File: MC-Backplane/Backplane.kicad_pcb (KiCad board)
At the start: 4 copper layers, 274.3 x 132.6 mm, 54 parts, among them J1 1730010, U1 64600001223, U10 86094328314755V1LF, U11 86094328314755V1LF, U12 374472, U13 86094328314755V1LF, U14 86094328314755V1LF, U2 SISS05DN-T1-GE3, U3 86094328314755V1LF, U4 86094328314755V1LF, U5 86094328314755V1LF, U6 86094328314755V1LF, U7 86094328314755V1LF, U8 86094328314755V1LF, U9 86094328314755V1LF

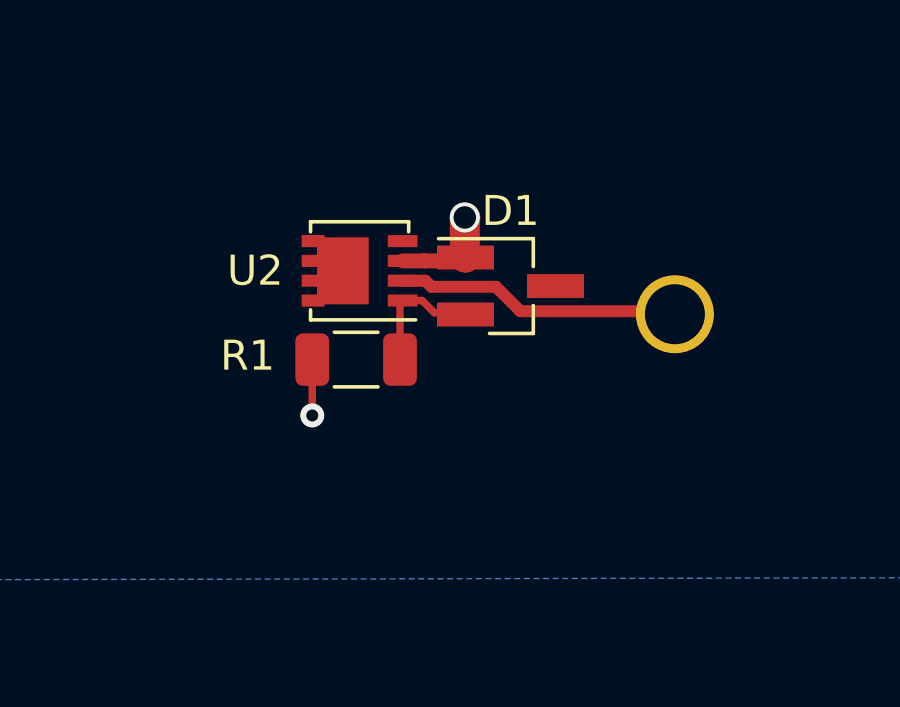
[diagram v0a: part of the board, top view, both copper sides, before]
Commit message: - updated PMOSFET&Zener footprint
reverse polarity protection circuit
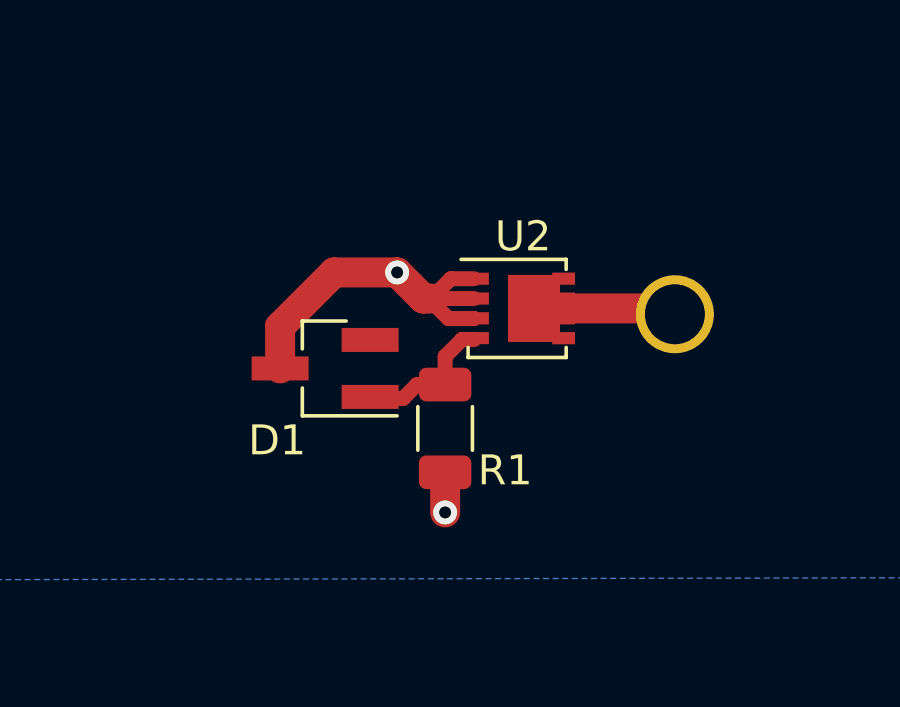
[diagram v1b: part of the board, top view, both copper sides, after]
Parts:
- moved D1 6.76 mm to (79.2, 139.0), turned to 180 degrees
- moved U2 5.40 mm to (85.6, 137.0), turned to 0 degrees
- moved R1 3.75 mm to (83.2, 141.0), turned to 270 degrees
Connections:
- D1 pad 1: /24V -> Net-(D1-Pad1)
- D1 pad 3: (no net) -> /24V
- R1 pad 1: Net-(D1-Pad2) -> Net-(D1-Pad1)
- U2 pad 1: Net-(D1-Pad2) -> /24V
- U2 pad 2: Net-(U1-Pad2) -> /24V
- U2 pad 4: (no net) -> Net-(D1-Pad1)
- U2 pad 5: (no net) -> Net-(U1-Pad2)
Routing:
- net /24V: track 4.83 -> 14.0 mm
- net Net-(D1-Pad1): track 0.00 -> 4.85 mm
- net Net-(U1-Pad2): track 9.65 -> 4.96 mm
- net Net-(D1-Pad2): track 4.52 -> 0.00 mm
- net /GND: track 80.2 -> 79.5 mm

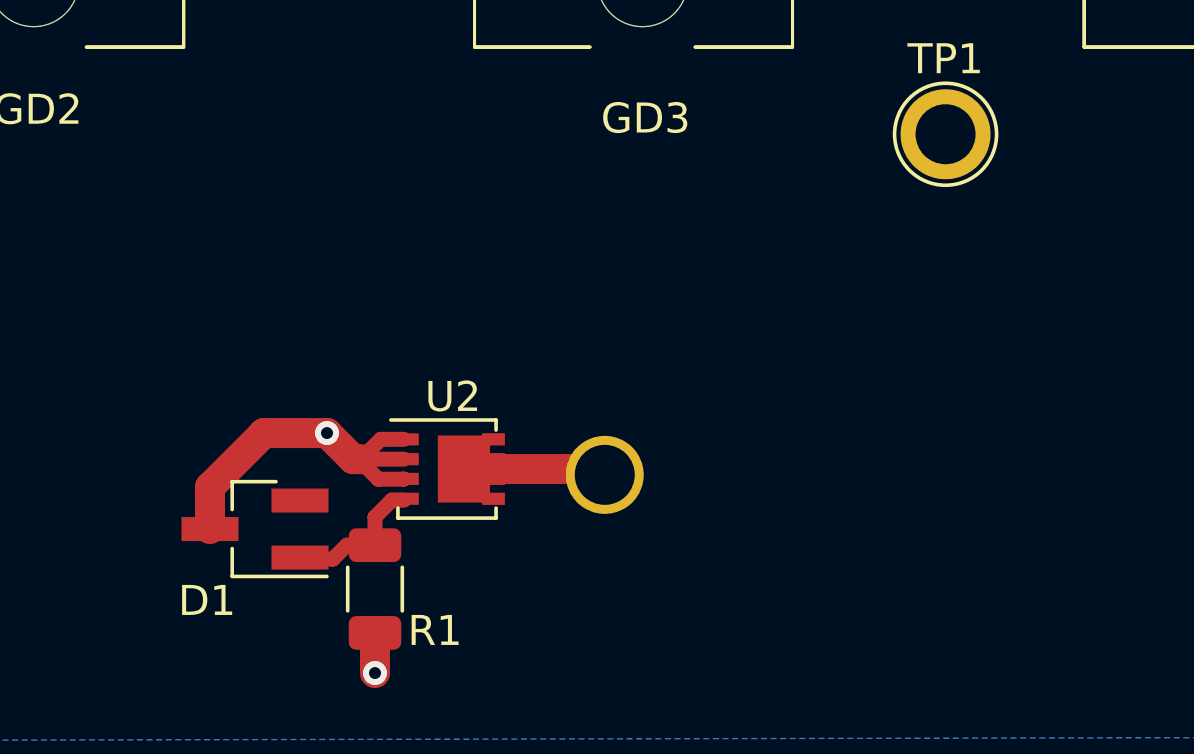
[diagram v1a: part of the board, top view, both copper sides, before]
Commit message: increased 24V trace width.
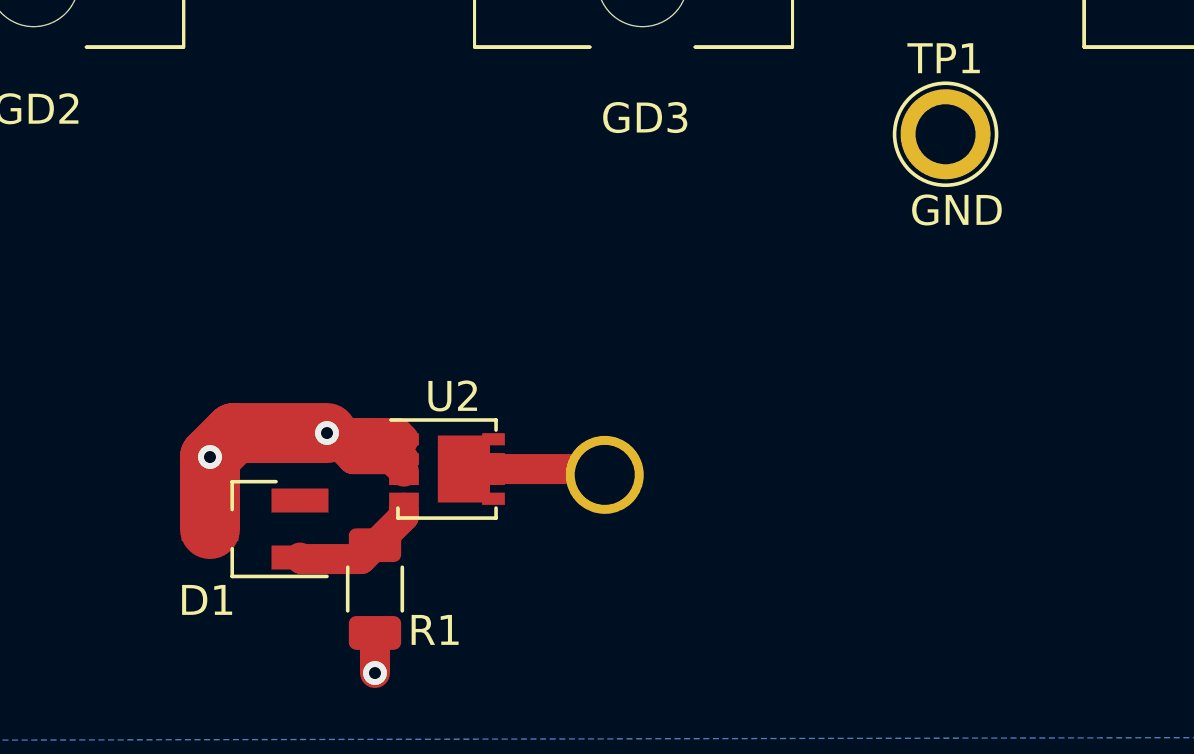
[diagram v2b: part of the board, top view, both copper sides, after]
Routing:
- net /24V: track 14.0 -> 17.1 mm, vias 1 -> 2
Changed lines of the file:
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@@
   (general
     (thickness 1.6)
-    (drawings 75)
+    (drawings 76)
     (tracks 540)
     (zones 0)
@@
   )
   (setup
-    (last_trace_width 1)
+    (last_trace_width 0.25)
     (user_trace_width 0.5)
     (user_trace_width 1)
+    (user_trace_width 2)
     (trace_clearance 0.2)
     (zone_clearance 0.508)
@@
       (net 4 /GND))
   )
+  (gr_text GND (at 102.5778 128.4044) (layer F.SilkS)
+    (effects (font (size 1 1) (thickness 0.15)))
+  )
   (gr_text "Backplane\nSenior Design Project 20: Modular Computer\nJulia Germano, Jacob Williams, Zach Murray\n2021-2022" (at 279.5016 135.4201) (layer F.SilkS)
     (effects (font (size 1 1) (thickness 0.15)))
@@
   (segment (start 117.9195 137.1092) (end 117.8814 137.1473) (width 1) (layer F.Cu) (net 1))
   (segment (start 123.1049 137.1092) (end 117.9195 137.1092) (width 1) (layer F.Cu) (net 1))
-  (segment (start 84.1428 136.6744) (end 82.7078 136.6744) (width 0.5) (layer F.Cu) (net 3))
+  (segment (start 82.1778 135.8044) (end 81.577802 135.8044) (width 1) (layer F.Cu) (net 3))
+  (segment (start 82.855301 135.8044) (end 82.1778 135.8044) (width 1) (layer F.Cu) (net 3))
+  (segment (start 83.2728 135.8044) (end 82.1778 135.8044) (width 1) (layer F.Cu) (net 3))
+  (segment (start 81.577802 135.8044) (end 81.577776 135.8044) (width 0.5) (layer F.Cu) (net 3))
+  (segment (start 83.9328 135.8044) (end 82.1778 135.8044) (width 1) (layer F.Cu) (net 3))
+  (segment (start 84.1428 136.0144) (end 83.9328 135.8044) (width 1) (layer F.Cu) (net 3))
   (segment (start 82.4478 136.6744) (end 81.5778 135.8044) (width 1) (layer F.Cu) (net 3))
-  (segment (start 82.7078 136.6744) (end 82.4478 136.6744) (width 1) (layer F.Cu) (net 3))
-  (segment (start 77.6778 137.6044) (end 79.4778 135.8044) (width 1) (layer F.Cu) (net 3))
-  (segment (start 77.6778 139.0044) (end 77.6778 137.6044) (width 1) (layer F.Cu) (net 3))
-  (segment (start 79.4778 135.8044) (end 81.5778 135.8044) (width 1) (layer F.Cu) (net 3))
-  (via (at 81.5778 135.8044) (size 0.8) (drill 0.4) (layers F.Cu B.Cu) (net 3))
-  (segment (start 81.8378 135.8044) (end 81.5778 135.8044) (width 0.5) (layer F.Cu) (net 3))
-  (segment (start 82.7078 136.6744) (end 81.8378 135.8044) (width 0.5) (layer F.Cu) (net 3))
-  (segment (start 82.66405 136.71815) (end 83.287799 137.341899) (width 0.5) (layer F.Cu) (net 3))
-  (segment (start 84.135301 137.341899) (end 84.1428 137.3344) (width 0.5) (layer F.Cu) (net 3))
-  (segment (start 83.3678 136.0144) (end 82.66405 136.71815) (width 0.5) (layer F.Cu) (net 3))
-  (segment (start 83.287799 137.341899) (end 84.135301 137.341899) (width 0.5) (layer F.Cu) (net 3))
-  (segment (start 84.1428 136.0144) (end 83.3678 136.0144) (width 0.5) (layer F.Cu) (net 3))
+  (segment (start 84.1428 136.6744) (end 82.4478 136.6744) (width 1) (layer F.Cu) (net 3))
+  (segment (start 82.855301 135.8044) (end 84.1428 137.091899) (width 1) (layer F.Cu) (net 3))
+  (segment (start 81.577776 135.8044) (end 82.855301 135.8044) (width 1) (layer F.Cu) (net 3))
+  (via (at 81.577776 135.8044) (size 0.8) (drill 0.4) (layers F.Cu B.Cu) (net 3))
+  (segment (start 78.4778 135.8044) (end 81.577776 135.8044) (width 2) (layer F.Cu) (net 3))
+  (segment (start 77.6778 136.6044) (end 78.4778 135.8044) (width 2) (layer F.Cu) (net 3))
+  (via (at 77.6778 136.6044) (size 0.8) (drill 0.4) (layers F.Cu B.Cu) (net 3))
+  (segment (start 77.6778 137.7044) (end 77.6778 136.6044) (width 2) (layer F.Cu) (net 3))
+  (segment (start 77.6778 139.0044) (end 77.6778 137.7044) (width 2) (layer F.Cu) (net 3))
   (segment (start 226.187 117.348) (end 226.1362 117.348) (width 0.25) (layer F.Cu) (net 4))
   (via (at 83.1778 143.8044) (size 0.8) (drill 0.4) (layers F.Cu B.Cu) (net 4))
@@
   (segment (start 93.218 93.3704) (end 94.3356 94.488) (width 0.25) (layer F.Cu) (net 72))
   (segment (start 74.041 94.488) (end 75.1586 93.3704) (width 0.25) (layer F.Cu) (net 72))
-  (segment (start 83.740291 138.041909) (end 84.1428 138.041909) (width 0.5) (layer F.Cu) (net 73))
-  (segment (start 83.1778 138.6044) (end 83.740291 138.041909) (width 0.5) (layer F.Cu) (net 73))
-  (segment (start 83.1778 139.5419) (end 83.1778 138.6044) (width 0.5) (layer F.Cu) (net 73))
-  (segment (start 80.7278 140.0044) (end 80.6778 139.9544) (width 0.5) (layer F.Cu) (net 73))
-  (segment (start 81.7778 140.0044) (end 80.7278 140.0044) (width 0.5) (layer F.Cu) (net 73))
-  (segment (start 82.2403 139.5419) (end 81.7778 140.0044) (width 0.5) (layer F.Cu) (net 73))
-  (segment (start 83.1778 139.5419) (end 82.2403 139.5419) (width 0.5) (layer F.Cu) (net 73))
+  (segment (start 84.1428 138.5769) (end 84.1428 138.291908) (width 1) (layer F.Cu) (net 73))
+  (segment (start 83.1778 139.5419) (end 84.1428 138.5769) (width 1) (layer F.Cu) (net 73))
+  (segment (start 80.7278 140.0044) (end 80.6778 139.9544) (width 1) (layer F.Cu) (net 73))
+  (segment (start 82.7153 140.0044) (end 80.7278 140.0044) (width 1) (layer F.Cu) (net 73))
+  (segment (start 83.1778 139.5419) (end 82.7153 140.0044) (width 1) (layer F.Cu) (net 73))
   (zone (net 4) (net_name /GND) (layer In2.Cu) (hatch edge 0.508)
     (connect_pads (clearance 0.508))
